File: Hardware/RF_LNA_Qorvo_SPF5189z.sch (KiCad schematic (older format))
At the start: 12 parts, among them U3 SPF5189Z

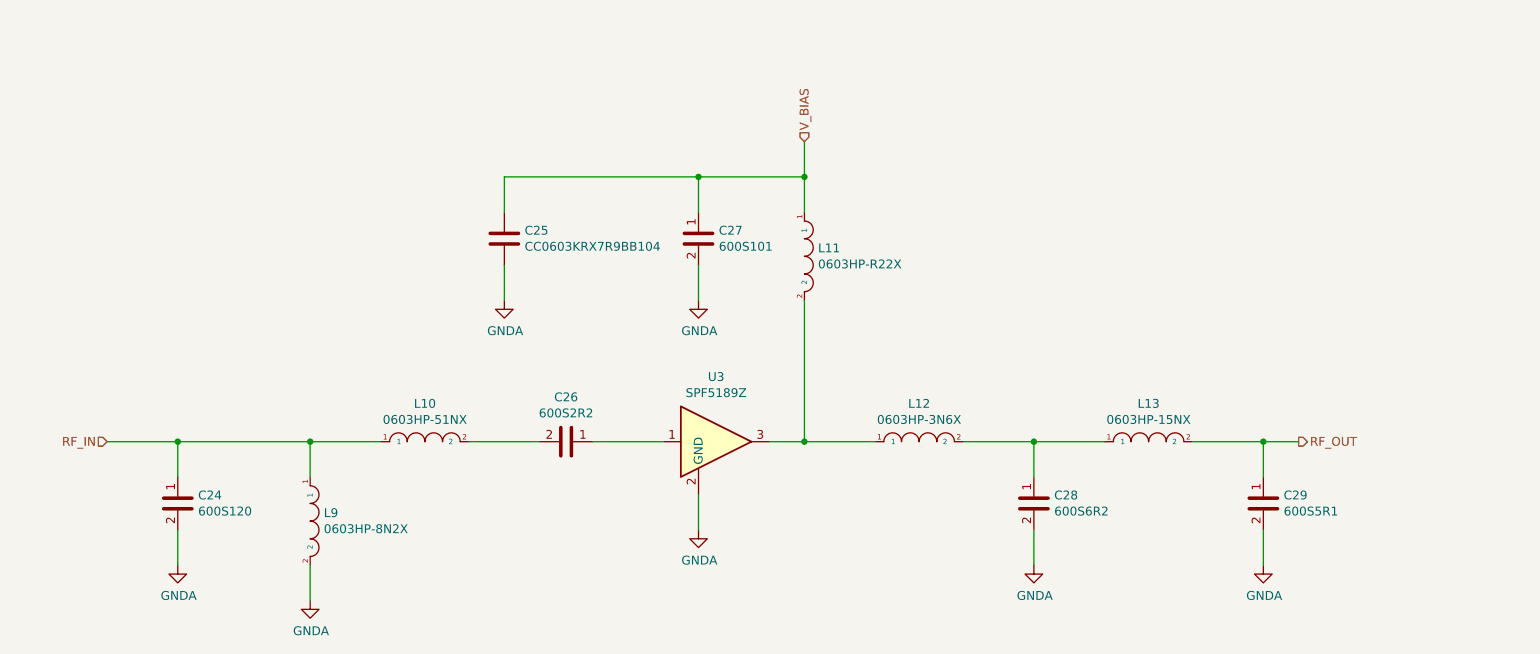
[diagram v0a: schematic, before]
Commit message: Added discrete Chebyshev input filter to schematic based on Qucs simulationd. Artwork not done. It has occurred to me that I need to do some major cleanup of the test points on this PCBA.
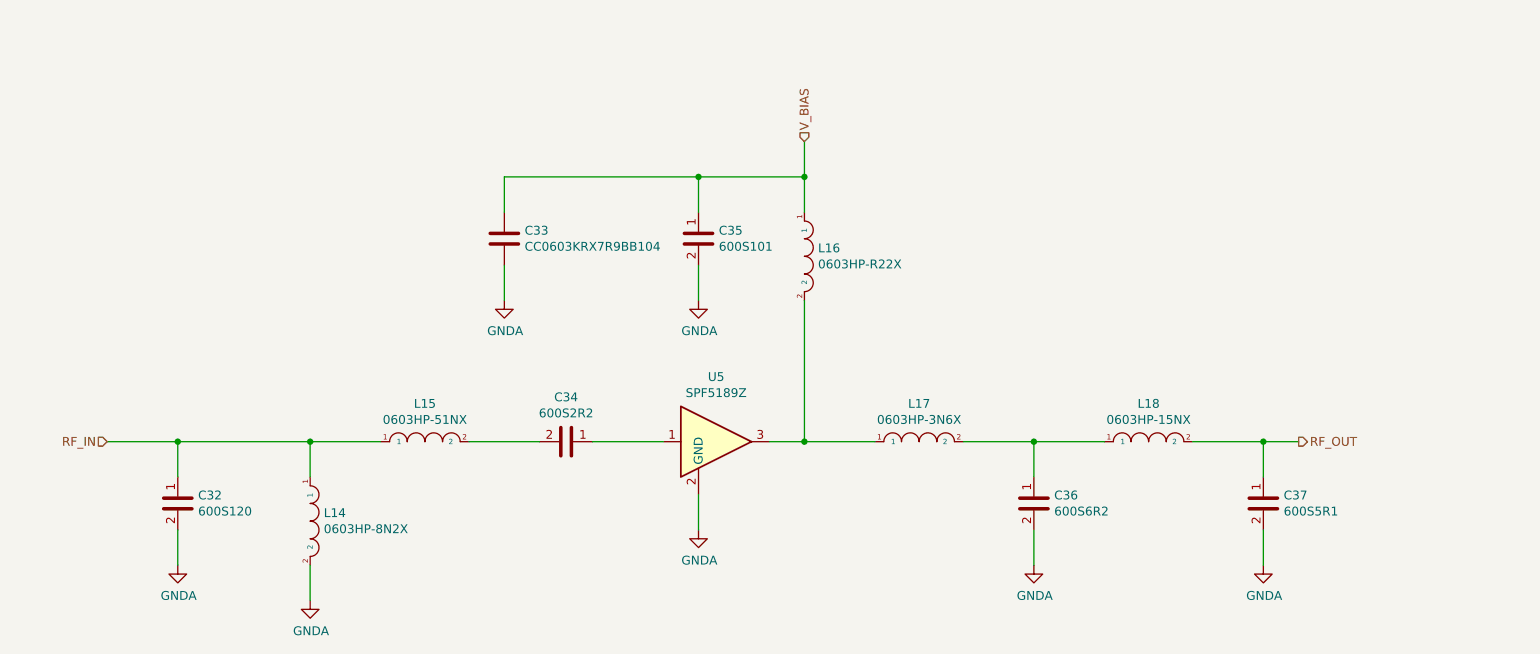
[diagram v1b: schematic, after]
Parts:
- renumbered C24 to C23, C25 to C24, C26 to C25, C27 to C26, C28 to C27, C29 to C28
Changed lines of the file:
@@
 $Descr A4 11693 8268
 encoding utf-8
-Sheet 8 12
+Sheet 8 16
 Title ""
 Date ""
@@
 AR Path="/503BB638/5F0481FC" Ref="#PWR?"  Part="1"
 AR Path="/5F1E02B6/5F0481FC" Ref="#PWR?"  Part="1"
-AR Path="/5F042EDC/5F0481FC" Ref="#PWR034"  Part="1"
+AR Path="/5F042EDC/5F0481FC" Ref="#PWR031"  Part="1"
 AR Path="/5F19ABE9/5F0481FC" Ref="#PWR?"  Part="1"
-AR Path="/5F21A108/5F0481FC" Ref="#PWR043"  Part="1"
-F 0 "#PWR043" H 3500 4950 50  0001 C CNN
+AR Path="/5F21A108/5F0481FC" Ref="#PWR040"  Part="1"
+F 0 "#PWR040" H 3500 4950 50  0001 C CNN
 F 1 "GNDA" H 3505 5027 50  0000 C CNN
 F 2 "" H 3500 5200 50  0001 C CNN
@@
 AR Path="/503BB638/5F048202" Ref="#PWR?"  Part="1"
 AR Path="/5F1E02B6/5F048202" Ref="#PWR?"  Part="1"
-AR Path="/5F042EDC/5F048202" Ref="#PWR037"  Part="1"
+AR Path="/5F042EDC/5F048202" Ref="#PWR034"  Part="1"
 AR Path="/5F19ABE9/5F048202" Ref="#PWR?"  Part="1"
-AR Path="/5F21A108/5F048202" Ref="#PWR046"  Part="1"
-F 0 "#PWR046" H 5700 4550 50  0001 C CNN
+AR Path="/5F21A108/5F048202" Ref="#PWR043"  Part="1"
+F 0 "#PWR043" H 5700 4550 50  0001 C CNN
 F 1 "GNDA" H 5705 4627 50  0000 C CNN
 F 2 "" H 5700 4800 50  0001 C CNN
@@
 AR Path="/503BB638/5F04820E" Ref="#PWR?"  Part="1"
 AR Path="/5F1E02B6/5F04820E" Ref="#PWR?"  Part="1"
-AR Path="/5F042EDC/5F04820E" Ref="#PWR038"  Part="1"
+AR Path="/5F042EDC/5F04820E" Ref="#PWR035"  Part="1"
 AR Path="/5F19ABE9/5F04820E" Ref="#PWR?"  Part="1"
-AR Path="/5F21A108/5F04820E" Ref="#PWR047"  Part="1"
-F 0 "#PWR047" H 7600 4750 50  0001 C CNN
+AR Path="/5F21A108/5F04820E" Ref="#PWR044"  Part="1"
+F 0 "#PWR044" H 7600 4750 50  0001 C CNN
 F 1 "GNDA" H 7605 4827 50  0000 C CNN
 F 2 "" H 7600 5000 50  0001 C CNN
@@
 AR Path="/5F19ABE9/5F048267" Ref="U?"  Part="1"
 AR Path="/5F21A108/5F048267" Ref="U5"  Part="1"
-F 0 "U3" H 5800 4667 50  0000 C CNN
+F 0 "U5" H 5800 4667 50  0000 C CNN
 F 1 "SPF5189Z" H 5800 4576 50  0000 C CNN
 F 2 "RF:SOT-89-3_Qorvo_SPF5189z" H 5850 4700 50  0001 C CNN
@@
 AR Path="/503BB638/5F0C1A3D" Ref="#PWR?"  Part="1"
 AR Path="/5F1E02B6/5F0C1A3D" Ref="#PWR?"  Part="1"
-AR Path="/5F042EDC/5F0C1A3D" Ref="#PWR033"  Part="1"
+AR Path="/5F042EDC/5F0C1A3D" Ref="#PWR030"  Part="1"
 AR Path="/5F19ABE9/5F0C1A3D" Ref="#PWR?"  Part="1"
-AR Path="/5F21A108/5F0C1A3D" Ref="#PWR042"  Part="1"
-F 0 "#PWR042" H 2750 4750 50  0001 C CNN
+AR Path="/5F21A108/5F0C1A3D" Ref="#PWR039"  Part="1"
+F 0 "#PWR039" H 2750 4750 50  0001 C CNN
 F 1 "GNDA" H 2755 4827 50  0000 C CNN
 F 2 "" H 2750 5000 50  0001 C CNN
@@
 AR Path="/503BB638/5F0DEF0A" Ref="#PWR?"  Part="1"
 AR Path="/5F1E02B6/5F0DEF0A" Ref="#PWR?"  Part="1"
-AR Path="/5F042EDC/5F0DEF0A" Ref="#PWR039"  Part="1"
+AR Path="/5F042EDC/5F0DEF0A" Ref="#PWR036"  Part="1"
 AR Path="/5F19ABE9/5F0DEF0A" Ref="#PWR?"  Part="1"
-AR Path="/5F21A108/5F0DEF0A" Ref="#PWR048"  Part="1"
-F 0 "#PWR048" H 8900 4750 50  0001 C CNN
+AR Path="/5F21A108/5F0DEF0A" Ref="#PWR045"  Part="1"
+F 0 "#PWR045" H 8900 4750 50  0001 C CNN
 F 1 "GNDA" H 8905 4827 50  0000 C CNN
 F 2 "" H 8900 5000 50  0001 C CNN
@@
 AR Path="/503BB638/5F04824A" Ref="#PWR?"  Part="1"
 AR Path="/5F1E02B6/5F04824A" Ref="#PWR?"  Part="1"
-AR Path="/5F042EDC/5F04824A" Ref="#PWR036"  Part="1"
+AR Path="/5F042EDC/5F04824A" Ref="#PWR033"  Part="1"
 AR Path="/5F19ABE9/5F04824A" Ref="#PWR?"  Part="1"
-AR Path="/5F21A108/5F04824A" Ref="#PWR045"  Part="1"
-F 0 "#PWR045" H 5700 3250 50  0001 C CNN
+AR Path="/5F21A108/5F04824A" Ref="#PWR042"  Part="1"
+F 0 "#PWR042" H 5700 3250 50  0001 C CNN
 F 1 "GNDA" H 5705 3327 50  0000 C CNN
 F 2 "" H 5700 3500 50  0001 C CNN
@@
 AR Path="/503BB638/5F048243" Ref="#PWR?"  Part="1"
 AR Path="/5F1E02B6/5F048243" Ref="#PWR?"  Part="1"
-AR Path="/5F042EDC/5F048243" Ref="#PWR035"  Part="1"
+AR Path="/5F042EDC/5F048243" Ref="#PWR032"  Part="1"
 AR Path="/5F19ABE9/5F048243" Ref="#PWR?"  Part="1"
-AR Path="/5F21A108/5F048243" Ref="#PWR044"  Part="1"
-F 0 "#PWR044" H 4600 3250 50  0001 C CNN
+AR Path="/5F21A108/5F048243" Ref="#PWR041"  Part="1"
+F 0 "#PWR041" H 4600 3250 50  0001 C CNN
 F 1 "GNDA" H 4605 3327 50  0000 C CNN
 F 2 "" H 4600 3500 50  0001 C CNN
@@
 Connection ~ 2750 4300
 $Comp
-L ATC:600S120 C24
+L ATC:600S120 C23
 U 1 1 5F11EADA
 P 2750 4650
-AR Path="/5F042EDC/5F11EADA" Ref="C24"  Part="1"
+AR Path="/5F042EDC/5F11EADA" Ref="C23"  Part="1"
 AR Path="/5F19ABE9/5F11EADA" Ref="C?"  Part="1"
-AR Path="/5F21A108/5F11EADA" Ref="C33"  Part="1"
-F 0 "C24" H 2865 4696 50  0000 L CNN
+AR Path="/5F21A108/5F11EADA" Ref="C32"  Part="1"
+F 0 "C32" H 2865 4696 50  0000 L CNN
 F 1 "600S120" H 2865 4605 50  0000 L CNN
 F 2 "Capacitor_SMD:C_0603_1608Metric" H 2800 4750 50  0001 C CNN
@@
 AR Path="/5F19ABE9/5F11F298" Ref="L?"  Part="1"
 AR Path="/5F21A108/5F11F298" Ref="L14"  Part="1"
-F 0 "L9" V 3454 4827 50  0000 L CNN
+F 0 "L14" V 3454 4827 50  0000 L CNN
 F 1 "0603HP-8N2X" V 3545 4827 50  0000 L CNN
 F 2 "Resistor_SMD:R_0603_1608Metric" H 3250 4900 50  0001 C CNN
@@
 AR Path="/5F19ABE9/5F11F8DC" Ref="L?"  Part="1"
 AR Path="/5F21A108/5F11F8DC" Ref="L15"  Part="1"
-F 0 "L10" H 4150 4515 50  0000 C CNN
+F 0 "L15" H 4150 4515 50  0000 C CNN
 F 1 "0603HP-51NX" H 4150 4424 50  0000 C CNN
 F 2 "Resistor_SMD:R_0603_1608Metric" H 3900 4450 50  0001 C CNN
@@
 $EndComp
 $Comp
-L ATC:600S2R2 C26
+L ATC:600S2R2 C25
 U 1 1 5F120D64
 P 4950 4300
-AR Path="/5F042EDC/5F120D64" Ref="C26"  Part="1"
+AR Path="/5F042EDC/5F120D64" Ref="C25"  Part="1"
 AR Path="/5F19ABE9/5F120D64" Ref="C?"  Part="1"
-AR Path="/5F21A108/5F120D64" Ref="C35"  Part="1"
-F 0 "C26" V 4698 4300 50  0000 C CNN
+AR Path="/5F21A108/5F120D64" Ref="C34"  Part="1"
+F 0 "C34" V 4698 4300 50  0000 C CNN
 F 1 "600S2R2" V 4789 4300 50  0000 C CNN
 F 2 "Capacitor_SMD:C_0603_1608Metric" H 5000 4400 50  0001 C CNN
@@
 $EndComp
 $Comp
-L ATC:600S101 C27
+L ATC:600S101 C26
 U 1 1 5F123529
 P 5700 3150
-AR Path="/5F042EDC/5F123529" Ref="C27"  Part="1"
+AR Path="/5F042EDC/5F123529" Ref="C26"  Part="1"
 AR Path="/5F19ABE9/5F123529" Ref="C?"  Part="1"
-AR Path="/5F21A108/5F123529" Ref="C36"  Part="1"
-F 0 "C27" H 5815 3196 50  0000 L CNN
+AR Path="/5F21A108/5F123529" Ref="C35"  Part="1"
+F 0 "C35" H 5815 3196 50  0000 L CNN
 F 1 "600S101" H 5815 3105 50  0000 L CNN
 F 2 "Capacitor_SMD:C_0603_1608Metric" H 5750 3250 50  0001 C CNN
@@
 $EndComp
 $Comp
-L Yageo:CC0603KRX7R9BB104 C25
+L Yageo:CC0603KRX7R9BB104 C24
 U 1 1 5F123B00
 P 4600 3150
-AR Path="/5F042EDC/5F123B00" Ref="C25"  Part="1"
+AR Path="/5F042EDC/5F123B00" Ref="C24"  Part="1"
 AR Path="/5F19ABE9/5F123B00" Ref="C?"  Part="1"
-AR Path="/5F21A108/5F123B00" Ref="C34"  Part="1"
-F 0 "C25" H 4715 3196 50  0000 L CNN
+AR Path="/5F21A108/5F123B00" Ref="C33"  Part="1"
+F 0 "C33" H 4715 3196 50  0000 L CNN
 F 1 "CC0603KRX7R9BB104" H 4715 3105 50  0000 L CNN
 F 2 "Capacitor_SMD:C_0603_1608Metric" H 4638 3000 50  0001 C CNN
@@
 AR Path="/5F19ABE9/5F1240EB" Ref="L?"  Part="1"
 AR Path="/5F21A108/5F1240EB" Ref="L16"  Part="1"
-F 0 "L11" V 6254 3327 50  0000 L CNN
+F 0 "L16" V 6254 3327 50  0000 L CNN
 F 1 "0603HP-R22X" V 6345 3327 50  0000 L CNN
 F 2 "Resistor_SMD:R_0603_1608Metric" H 6050 3400 50  0001 C CNN
@@
 AR Path="/5F19ABE9/5F129BC1" Ref="L?"  Part="1"
 AR Path="/5F21A108/5F129BC1" Ref="L17"  Part="1"
-F 0 "L12" H 6950 4515 50  0000 C CNN
+F 0 "L17" H 6950 4515 50  0000 C CNN
 F 1 "0603HP-3N6X" H 6950 4424 50  0000 C CNN
 F 2 "Resistor_SMD:R_0603_1608Metric" H 6700 4450 50  0001 C CNN
@@
 $EndComp
 $Comp
-L ATC:600S6R2 C28
+L ATC:600S6R2 C27
 U 1 1 5F12A48C
 P 7600 4650
-AR Path="/5F042EDC/5F12A48C" Ref="C28"  Part="1"
+AR Path="/5F042EDC/5F12A48C" Ref="C27"  Part="1"
 AR Path="/5F19ABE9/5F12A48C" Ref="C?"  Part="1"
-AR Path="/5F21A108/5F12A48C" Ref="C37"  Part="1"
-F 0 "C28" H 7715 4696 50  0000 L CNN
+AR Path="/5F21A108/5F12A48C" Ref="C36"  Part="1"
+F 0 "C36" H 7715 4696 50  0000 L CNN
 F 1 "600S6R2" H 7715 4605 50  0000 L CNN
 F 2 "Capacitor_SMD:C_0603_1608Metric" H 7650 4750 50  0001 C CNN
@@
 AR Path="/5F19ABE9/5F12ADA0" Ref="L?"  Part="1"
 AR Path="/5F21A108/5F12ADA0" Ref="L18"  Part="1"
-F 0 "L13" H 8250 4515 50  0000 C CNN
+F 0 "L18" H 8250 4515 50  0000 C CNN
 F 1 "0603HP-15NX" H 8250 4424 50  0000 C CNN
 F 2 "Resistor_SMD:R_0603_1608Metric" H 8000 4450 50  0001 C CNN
@@
 $EndComp
 $Comp
-L ATC:600S5R1 C29
+L ATC:600S5R1 C28
 U 1 1 5F12BF23
 P 8900 4650
-AR Path="/5F042EDC/5F12BF23" Ref="C29"  Part="1"
+AR Path="/5F042EDC/5F12BF23" Ref="C28"  Part="1"
 AR Path="/5F19ABE9/5F12BF23" Ref="C?"  Part="1"
-AR Path="/5F21A108/5F12BF23" Ref="C38"  Part="1"
-F 0 "C29" H 9015 4696 50  0000 L CNN
+AR Path="/5F21A108/5F12BF23" Ref="C37"  Part="1"
+F 0 "C37" H 9015 4696 50  0000 L CNN
 F 1 "600S5R1" H 9015 4605 50  0000 L CNN
 F 2 "Capacitor_SMD:C_0603_1608Metric" H 8950 4750 50  0001 C CNN

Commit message: Major cleanup to both the schematic and directory structure. Stackup has changed accomodate to 0.65mm trace width. Chebyshev filter lived through the experience in the Qucs simulation; others not checked yet. I do want to re-visit the matching networks of all of the amplifiers as I have developed some good strategies to implement them.
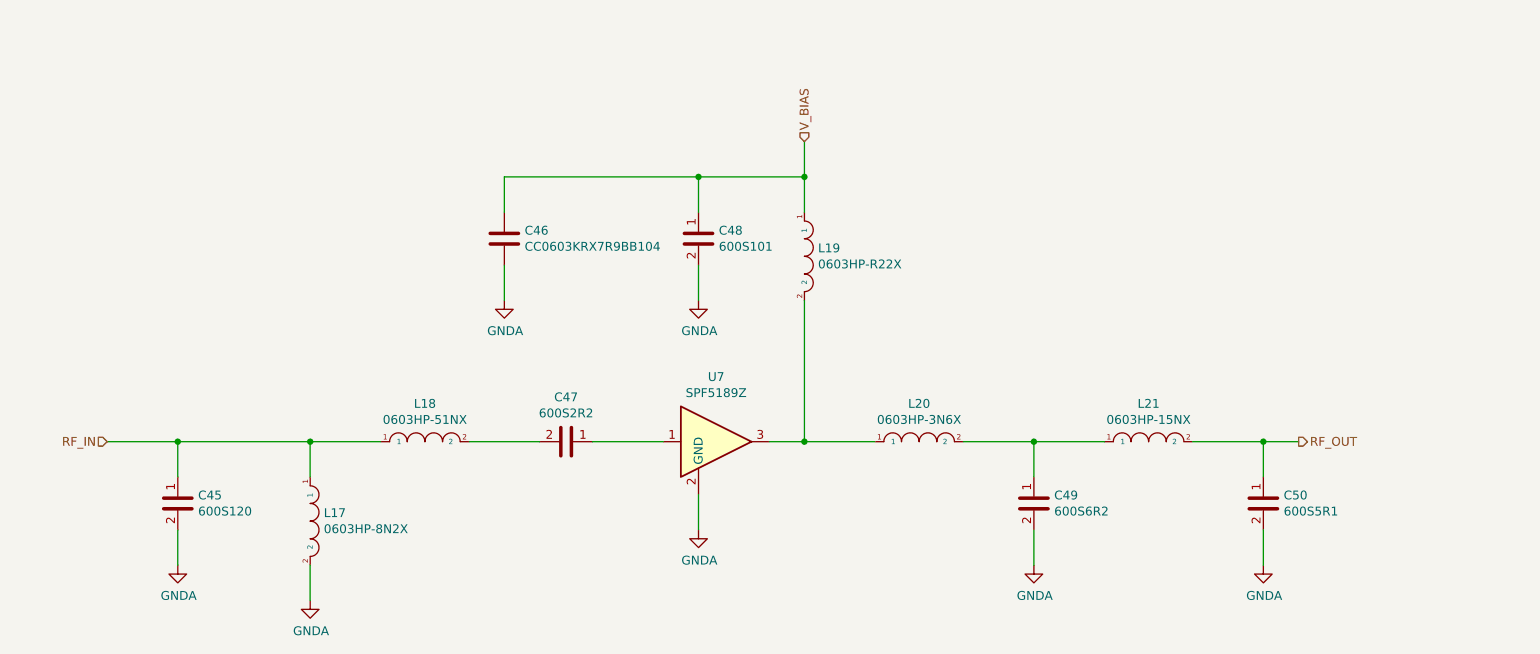
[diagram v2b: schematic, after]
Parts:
- renumbered C23 to C4, C24 to C5, C25 to C6, C26 to C7, C27 to C8, C28 to C9, L9 to L1, L10 to L2, L11 to L3, L12 to L4, L13 to L5, U3 to U2

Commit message: Improving LNA simulations and Documentation package. More to come on this one.
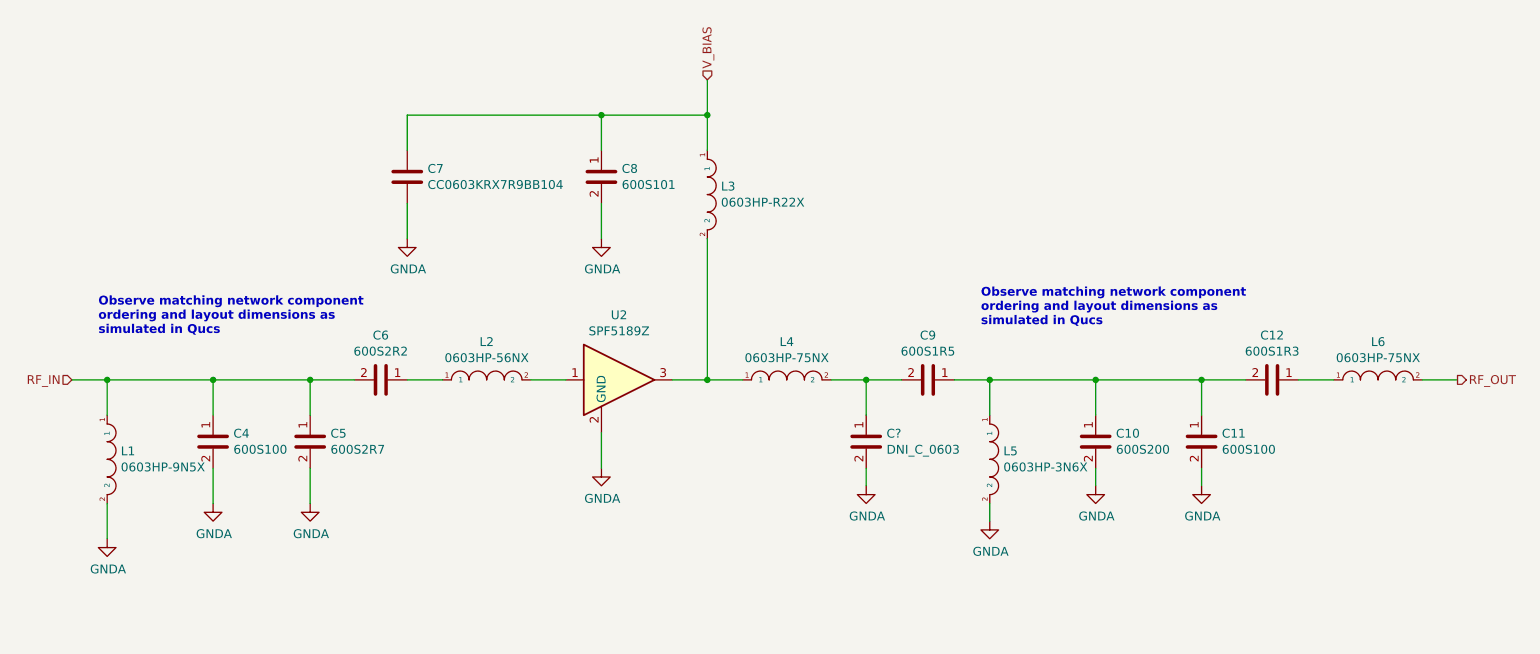
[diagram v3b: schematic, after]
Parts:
- removed C4: 600S120, Capacitor_SMD:C_0603_1608Metric, symbol ATC:600S120
- removed C8: 600S6R2, Capacitor_SMD:C_0603_1608Metric, symbol ATC:600S6R2
- removed C9: 600S5R1, Capacitor_SMD:C_0603_1608Metric, symbol ATC:600S5R1
- removed L1: 0603HP-8N2X, Resistor_SMD:R_0603_1608Metric, symbol Coilcraft:0603HP-8N2X
- removed L2: 0603HP-51NX, Resistor_SMD:R_0603_1608Metric, symbol Coilcraft:0603HP-51NX
- removed L4: 0603HP-3N6X, Resistor_SMD:R_0603_1608Metric, symbol Coilcraft:0603HP-3N6X
- removed L5: 0603HP-15NX, Resistor_SMD:R_0603_1608Metric, symbol Coilcraft:0603HP-15NX
- added C10: 600S200, Capacitor_SMD:C_0603_1608Metric, symbol ATC:600S200
- added C11, C4: 600S100, Capacitor_SMD:C_0603_1608Metric, symbol ATC:600S100
- added C12: 600S1R3, Capacitor_SMD:C_0603_1608Metric, symbol ATC:600S1R3
- added C5: 600S2R7, Capacitor_SMD:C_0603_1608Metric, symbol ATC:600S2R7
- added C9: 600S1R5, Capacitor_SMD:C_0603_1608Metric, symbol ATC:600S1R5
- added C?: DNI_C_0603, Capacitor_SMD:C_0603_1608Metric, symbol DNI:DNI_C_0603
- added L1: 0603HP-9N5X, Inductor_SMD:L_0603_1608Metric, symbol Coilcraft:0603HP-9N5X
- added L2: 0603HP-56NX, Inductor_SMD:L_0603_1608Metric, symbol Coilcraft:0603HP-56NX
- added L4, L6: 0603HP-75NX, Inductor_SMD:L_0603_1608Metric, symbol Coilcraft:0603HP-75NX
- added L5: 0603HP-3N6X, Inductor_SMD:L_0603_1608Metric, symbol Coilcraft:0603HP-3N6X
- renumbered C5 to C7, C7 to C8
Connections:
- net GNDA: now also C10.2, C11.2, C4.2, C5.2, C?.2, L1.2, L5.2
- net RF_IN: now also C6.2, C4.1, C5.1, L1.1
- net RF_OUT: now also L6.2
- net at U2.1: now also L2.2; no longer C6.1
- net at L3.2, U2.3: now also L4.1
- new net: C6.1, L2.1
- new net: C9.2, C?.1, L4.2
- new net: C10.1, C11.1, C12.2, C9.1, L5.1
- new net: C12.1, L6.1
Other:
- note added: "Observe matching network component\nordering and layout dimensions as\nsimulated in Qucs"
- moved on the sheet: C7, C8, L3, U2
